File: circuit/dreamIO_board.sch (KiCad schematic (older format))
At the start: 74 parts, among them IC1 TPS61200, P1 BATT, P2 CONN_01X08, P3 CONN_01X08, P4 CONN_01X02, P5 CONN_01X06, P6 gnd_con, P9 PixelOut, SW1 SPDT, SW2 RESET, SW3 PRGM, SW4 HCI2, SW5 HCI1, U1 MCP73831, U17 MPU-6050, U2 MICRO-B_USB, U4 ESP-12E

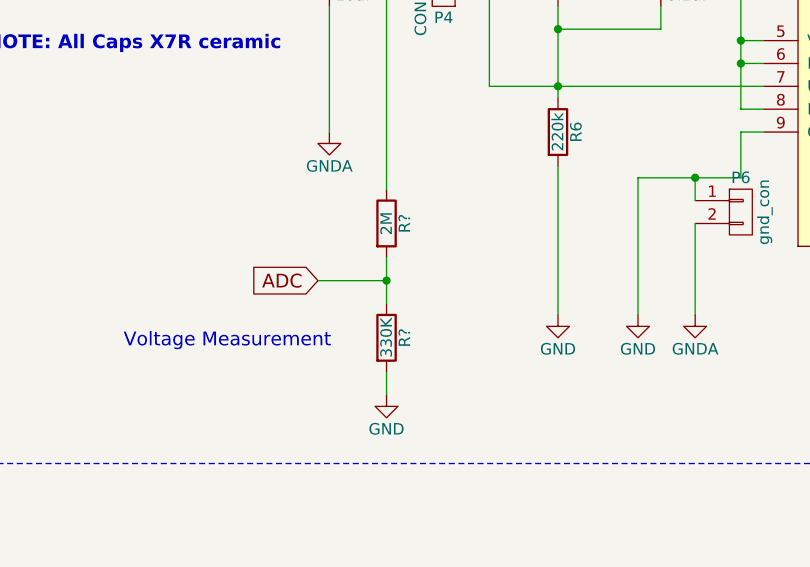
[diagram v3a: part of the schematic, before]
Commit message: had to add the bak and sch files for the circuit. not sure why they were not added before
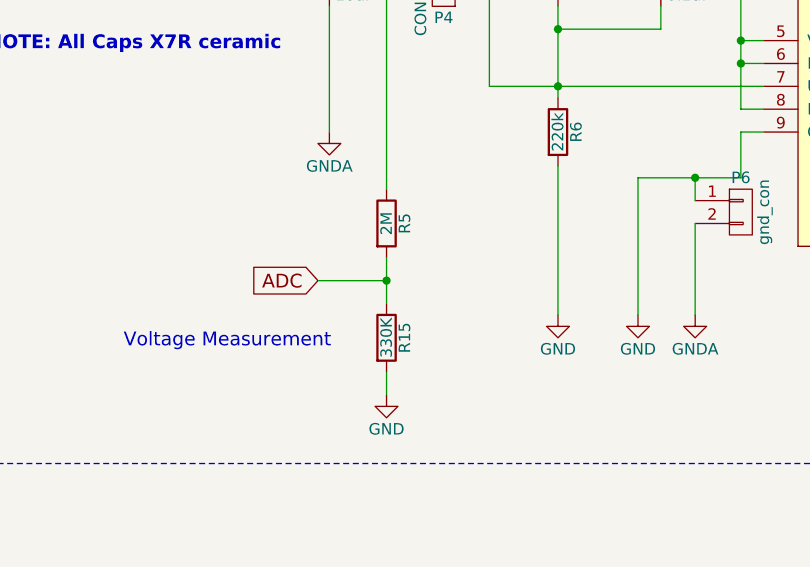
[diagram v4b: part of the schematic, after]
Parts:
- gave numbers to parts that had none: 2
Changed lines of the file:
@@
 Connection ~ 3050 2900
 $Comp
-L R R?
+L R R5
 U 1 1 57473836
 P 3050 4250
-F 0 "R?" V 3130 4250 50  0000 C CNN
+F 0 "R5" V 3130 4250 50  0000 C CNN
 F 1 "2M" V 3050 4250 50  0000 C CNN
 F 2 "kicad-libraries:0603" V 2980 4250 30  0001 C CNN
@@
 $EndComp
 $Comp
-L R R?
+L R R15
 U 1 1 5747458A
 P 3050 4750
-F 0 "R?" V 3130 4750 50  0000 C CNN
+F 0 "R15" V 3130 4750 50  0000 C CNN
 F 1 "330K" V 3050 4750 50  0000 C CNN
 F 2 "kicad-libraries:0603" V 2980 4750 30  0001 C CNN
@@
 $EndComp
 $Comp
-L GND #PWR?
+L GND #PWR048
 U 1 1 57474715
 P 3050 5000
-F 0 "#PWR?" H 3050 4750 50  0001 C CNN
+F 0 "#PWR048" H 3050 4750 50  0001 C CNN
 F 1 "GND" H 3050 4850 50  0000 C CNN
 F 2 "" H 3050 5000 50  0000 C CNN

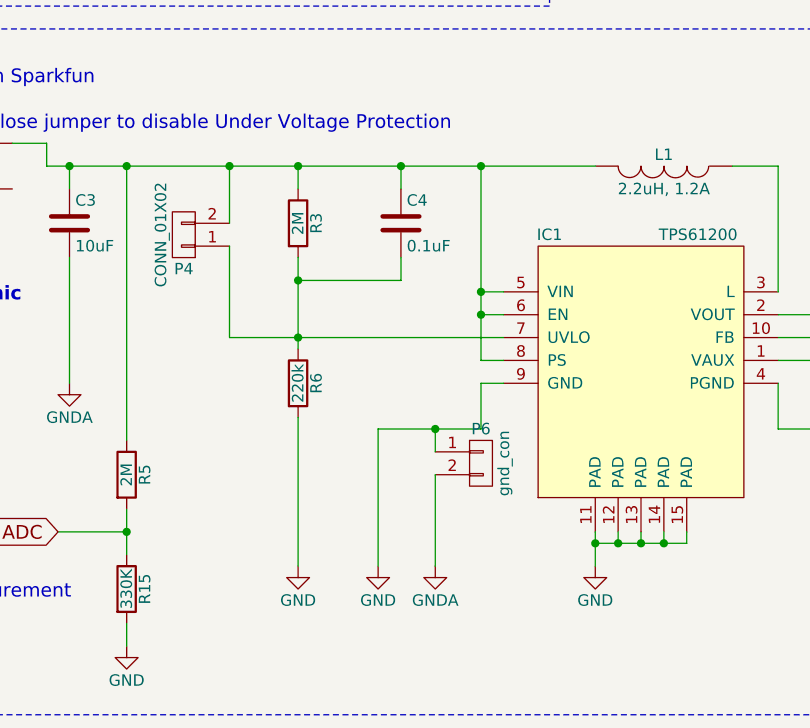
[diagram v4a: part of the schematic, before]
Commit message: removed a (seemingly) extra capacitor from TPS section. Emulated the layout for TPS from datasheet. roughly 40 connections to go. wooooo!
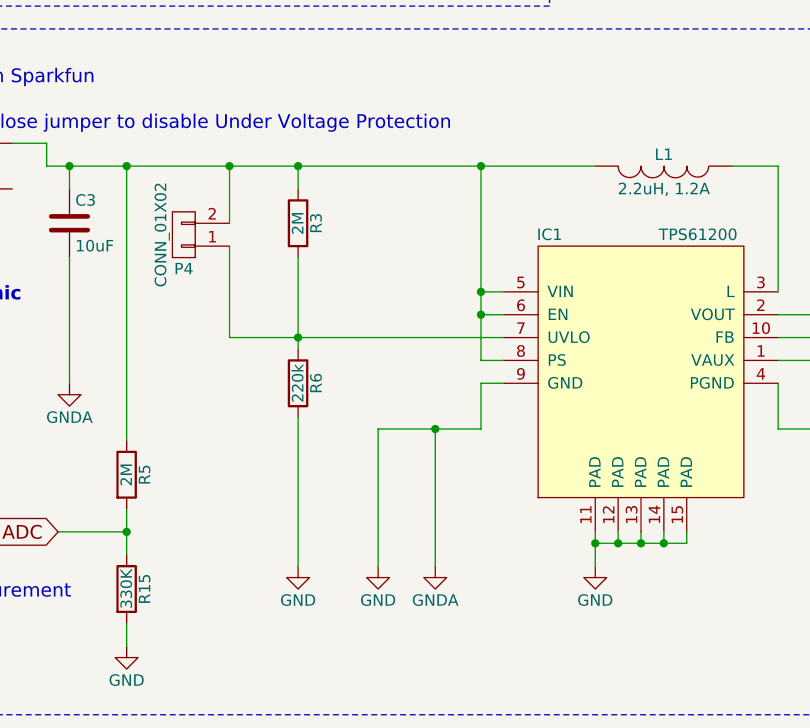
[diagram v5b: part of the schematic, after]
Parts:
- removed C4: 0.1uF, kicad-libraries:0603, symbol C
- removed P6: gnd_con, _connectors:_Solder_Pad2.54_2, symbol CONN_01X02
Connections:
- net GNDA is gone; now on net GND: C3.2, C5.2, C6.2, IC1.4 (PGND), R7.2
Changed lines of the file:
@@
-$EndComp
-$Comp
-L C C4
-U 1 1 56B06545
-P 4250 3150
-F 0 "C4" H 4275 3250 50  0000 L CNN
-F 1 "0.1uF" H 4275 3050 50  0000 L CNN
-F 2 "kicad-libraries:0603" H 4288 3000 30  0001 C CNN
-F 3 "" H 4250 3150 60  0000 C CNN
-	1    4250 3150
-	1    0    0    -1
 $EndComp
 $Comp
@@
 F 3 "" H 4150 4650 60  0000 C CNN
 	1    4150 4650
-	1    0    0    -1
-$EndComp
-$Comp
-L CONN_01X02 P6
-U 1 1 56E65EA0
-P 4600 4200
-F 0 "P6" H 4600 4350 50  0000 C CNN
-F 1 "gnd_con" V 4700 4200 50  0000 C CNN
-F 2 "_connectors:_Solder_Pad2.54_2" H 4600 4200 60  0001 C CNN
-F 3 "" H 4600 4200 60  0000 C CNN
-	1    4600 4200
 	1    0    0    -1
 $EndComp
@@
 	2800 8900 2800 9100
 Wire Wire Line
-	4400 4250 4400 4650
+	4400 4050 4400 4650
 Connection ~ 4400 4050
-Wire Wire Line
-	4400 4050 4400 4150
 Wire Wire Line
 	4150 4050 4150 4650
@@
 Wire Wire Line
 	5100 4500 5100 4650
-Connection ~ 3800 3400
-Wire Wire Line
-	4250 3400 3800 3400
-Wire Wire Line
-	4250 3300 4250 3400
-Connection ~ 4250 2900
-Wire Wire Line
-	4250 2900 4250 3000
 Connection ~ 3500 2900
 Wire Wire Line

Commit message: fixed error on board: neopixel out did not have 3.3v output
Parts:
- P9: footprint Pin_Headers:Pin_Header_Straight_1x03 -> kicad-libraries:PIN_ARRAY_3X1
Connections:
- net VCC is gone; now on net +3V3: P9.1 (P1)
